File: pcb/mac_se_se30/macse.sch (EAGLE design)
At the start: 11 parts, among them J2 ATX24RH

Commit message: updated pcb
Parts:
- removed J7: (no value), atx_power_control:CONN_023.5MM-NO_SILK
- removed JP1: (no value), atx_power_control:PINHD-1X4
- added JP4: (no value), pinhead:PINHD-1X3
- JP2: device pinhead:PINHD-1X2 -> pinhead:PINHD-1X2/90
- JP3: device atx_power_control:PINHD-1X4 -> appleii:4PIN_FAN
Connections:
- new net N$2: JP3.2_VCC, JP4.2
- net +12V: now also JP4.1; no longer C2.1, JP1.3
- net +5V: now also C2.1, JP4.3; no longer JP3.3
- net GND: now also JP3.1_GND; no longer J7.2, JP1.4, JP3.4
- net N$5: no longer J7.1

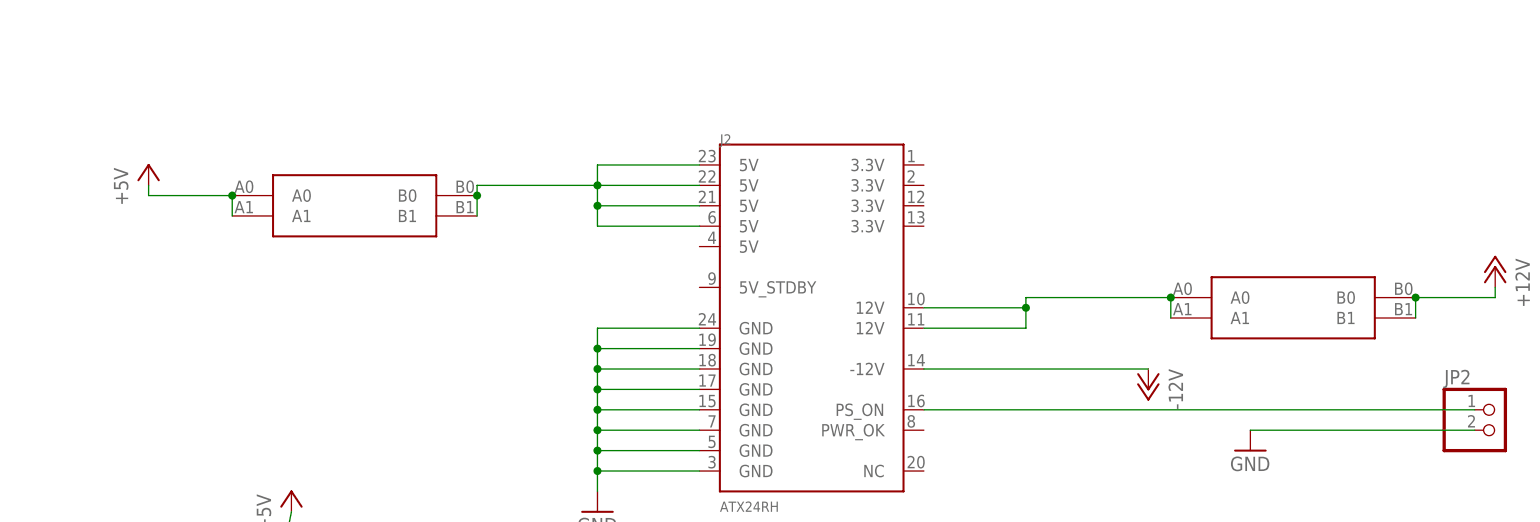
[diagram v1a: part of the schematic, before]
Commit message: added more caps
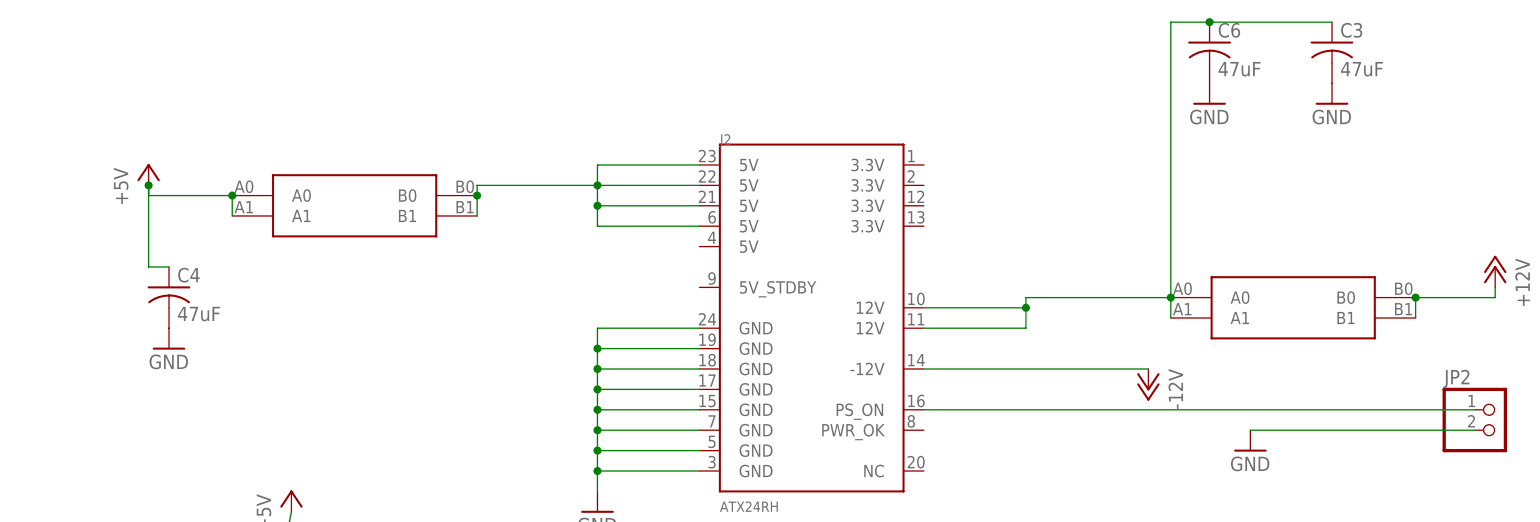
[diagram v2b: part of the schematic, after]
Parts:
- added C3, C4, C6: 47uF, clock:C-USC1210
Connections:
- net +5V: now also C4.1
- net GND: now also C3.2, C4.2, C6.2
- net N$8: now also C3.1, C6.1
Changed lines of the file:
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@@
 <?xml version="1.0" encoding="utf-8"?>
 <!DOCTYPE eagle SYSTEM "eagle.dtd">
-<eagle version="9.6.1">
+<eagle version="9.6.2">
 <drawing>
 <settings>
@@
 <part name="P+8" library="supply1" library_urn="urn:adsk.eagle:library:371" deviceset="+5V" device=""/>
 <part name="GND7" library="supply1" library_urn="urn:adsk.eagle:library:371" deviceset="GND" device=""/>
+<part name="C6" library="clock" deviceset="C-US" device="C1210" value="47uF"/>
+<part name="GND8" library="supply1" library_urn="urn:adsk.eagle:library:371" deviceset="GND" device=""/>
+<part name="GND9" library="supply1" library_urn="urn:adsk.eagle:library:371" deviceset="GND" device=""/>
+<part name="C3" library="clock" deviceset="C-US" device="C1210" value="47uF"/>
+<part name="C4" library="clock" deviceset="C-US" device="C1210" value="47uF"/>
+<part name="GND10" library="supply1" library_urn="urn:adsk.eagle:library:371" deviceset="GND" device=""/>
 </parts>
 <sheets>
@@
 <instance part="GND7" gate="1" x="27.94" y="124.46" smashed="yes">
 <attribute name="VALUE" x="25.4" y="121.92" size="1.778" layer="96"/>
+</instance>
+<instance part="C6" gate="G$1" x="144.78" y="208.28" smashed="yes">
+<attribute name="NAME" x="145.796" y="208.915" size="1.778" layer="95"/>
+<attribute name="VALUE" x="145.796" y="204.089" size="1.778" layer="96"/>
+</instance>
+<instance part="GND8" gate="1" x="144.78" y="200.66" smashed="yes">
+<attribute name="VALUE" x="142.24" y="198.12" size="1.778" layer="96"/>
+</instance>
+<instance part="GND9" gate="1" x="160.02" y="200.66" smashed="yes">
+<attribute name="VALUE" x="157.48" y="198.12" size="1.778" layer="96"/>
+</instance>
+<instance part="C3" gate="G$1" x="160.02" y="208.28" smashed="yes">
+<attribute name="NAME" x="161.036" y="208.915" size="1.778" layer="95"/>
+<attribute name="VALUE" x="161.036" y="204.089" size="1.778" layer="96"/>
+</instance>
+<instance part="C4" gate="G$1" x="15.24" y="177.8" smashed="yes">
+<attribute name="NAME" x="16.256" y="178.435" size="1.778" layer="95"/>
+<attribute name="VALUE" x="16.256" y="173.609" size="1.778" layer="96"/>
+</instance>
+<instance part="GND10" gate="1" x="15.24" y="170.18" smashed="yes">
+<attribute name="VALUE" x="12.7" y="167.64" size="1.778" layer="96"/>
 </instance>
 </instances>
@@
 <wire x1="27.94" y1="127" x2="27.94" y2="129.54" width="0.1524" layer="91"/>
 </segment>
+<segment>
+<pinref part="C6" gate="G$1" pin="2"/>
+<pinref part="GND8" gate="1" pin="GND"/>
+</segment>
+<segment>
+<pinref part="GND9" gate="1" pin="GND"/>
+<pinref part="C3" gate="G$1" pin="2"/>
+</segment>
+<segment>
+<pinref part="C4" gate="G$1" pin="2"/>
+<pinref part="GND10" gate="1" pin="GND"/>
+</segment>
 </net>
 <net name="-12V" class="0">
@@
 <wire x1="12.7" y1="189.23" x2="12.7" y2="190.5" width="0.1524" layer="91"/>
 <junction x="23.114" y="189.23"/>
+<pinref part="C4" gate="G$1" pin="1"/>
+<wire x1="12.7" y1="190.5" x2="12.7" y2="180.34" width="0.1524" layer="91"/>
+<wire x1="12.7" y1="180.34" x2="15.24" y2="180.34" width="0.1524" layer="91"/>
+<junction x="12.7" y="190.5"/>
 </segment>
 <segment>
@@
 <pinref part="J2" gate="G$1" pin="12V@0"/>
 <pinref part="J2" gate="G$1" pin="12V@1"/>
+<pinref part="C6" gate="G$1" pin="1"/>
+<wire x1="160.02" y1="210.82" x2="144.78" y2="210.82" width="0.1524" layer="91"/>
+<wire x1="139.954" y1="176.53" x2="139.954" y2="210.82" width="0.1524" layer="91"/>
+<wire x1="139.954" y1="210.82" x2="144.78" y2="210.82" width="0.1524" layer="91"/>
+<junction x="144.78" y="210.82"/>
+<pinref part="C3" gate="G$1" pin="1"/>
 </segment>
 </net>

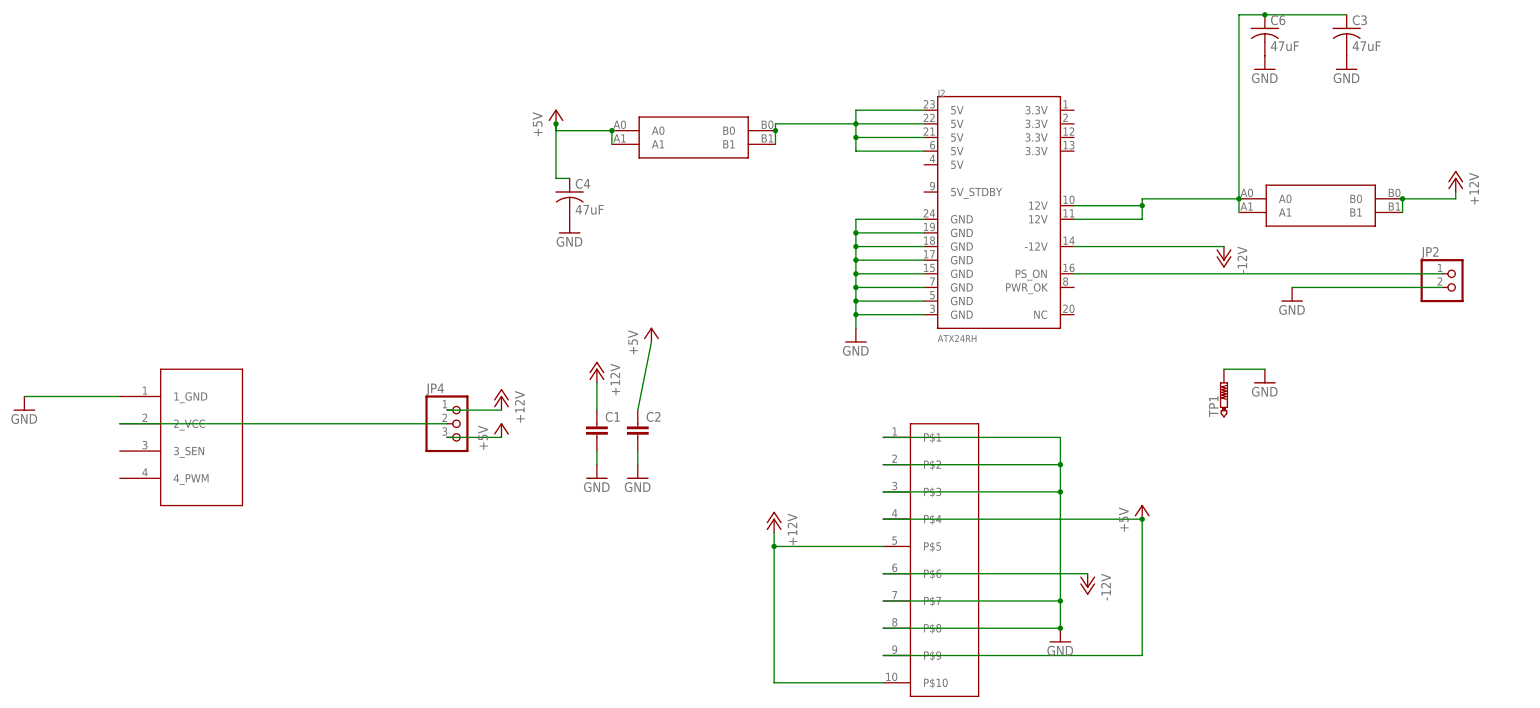
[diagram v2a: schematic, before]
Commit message: added more caps
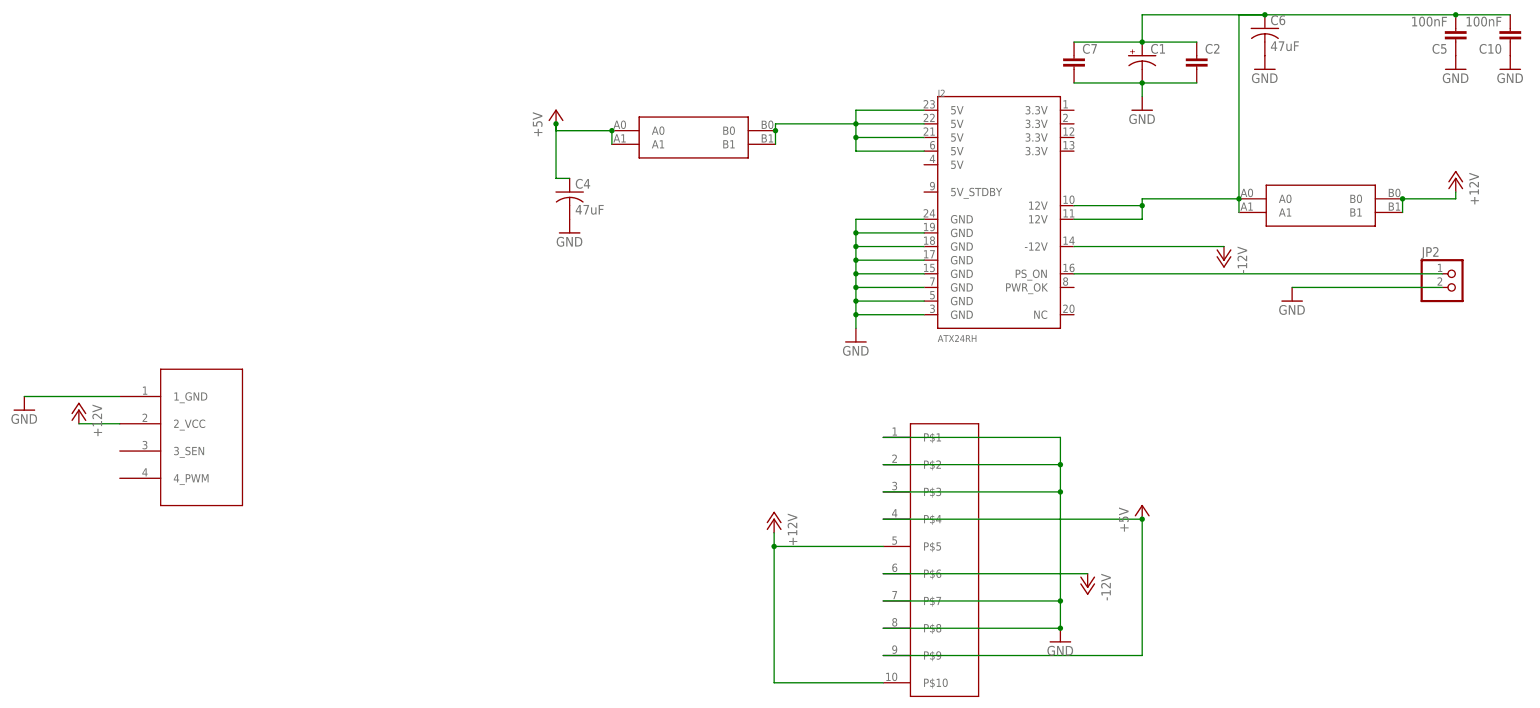
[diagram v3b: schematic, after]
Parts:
- removed C3: 47uF, clock:C-USC1210
- removed JP4: (no value), pinhead:PINHD-1X3
- removed TP1: PTR1PAD1-20Y, testpad:PTR1PAD1-20Y
- added C10, C5: 100nF, clock:CAP0805
- added C7: (no value), capacitor-wima:C5/2.5
- C1: device capacitor-wima:C5/2.5 -> adafruit_changed:CPOL-USE3.5-8
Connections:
- removed net N$2: JP3.2_VCC, JP4.2
- net +12V: now also JP3.2_VCC; no longer C1.1, JP4.1
- net +5V: no longer C2.1, JP4.3
- net GND: now also C1.-, C10.1, C5.1, C7.2; no longer C1.2, C3.2, TP1.TP
- net N$8: now also C1.+, C10.2, C2.1, C5.2, C7.1; no longer C3.1
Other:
- moved on the sheet: C2
